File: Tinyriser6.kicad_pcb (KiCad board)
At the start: 4 copper layers, 113.2 x 23.5 mm, 25 parts, among them J1 Bus_M.2_Socket_M, J2 Bus_PCI_Express_x16, J3 Conn_02x04_Odd_Even, J6 USB_A, J7 Conn_02x10_Odd_Even, M1 Fan_4pin

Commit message: finished connecting pretty much all of the random io
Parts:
- moved J7 18.1 mm to (184.2, 66.0), turned to -90 degrees
- moved TP3 8.30 mm to (155.6, 55.5)
- moved TP7 8.30 mm to (155.6, 58.5)
- moved G*** 3.95 mm to (139.9, 66.5) (x2)
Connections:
- J7 pad 1: RSMRST_SIO# -> GND
- J7 pad 10: PWRBTN# -> PCIe_CPU_REFCLK11+
- J7 pad 11: PCIe_CPU_REFCLK11+ -> PWRBTN#
- J7 pad 12: ME_RECOVERY_BMC -> PCIe_CPU_REFCLK11-
- J7 pad 13: FP_RST# -> AZ_SDOUT_R
- J7 pad 14: SMLINK1_DATA -> SIO_SML1ALERT#
- J7 pad 15: SMLINK1_CLK -> GPU_PWR_EN
- J7 pad 16: PCIE_X8_X4_PRSNT# -> GPU_MACO_EN
- J7 pad 17: +3V3_S5 -> PCH_SYSPOWEROK
- J7 pad 18: +3V3 -> BMC_DETECT#
- J7 pad 19: GND -> +5V
- J7 pad 2: +5V -> GND
- J7 pad 20: GND -> RSMRST_SIO#
- J7 pad 3: BMC_DETECT# -> +3V3
- J7 pad 4: PCH_SYSPOWEROK -> +3V3_S5
- J7 pad 5: GPU_MACO_EN -> PCIE_X8_X4_PRSNT#
- J7 pad 6: GPU_PWR_EN -> SMLINK1_CLK
- J7 pad 7: SIO_SML1ALERT# -> SMLINK1_DATA
- J7 pad 8: AZ_SDOUT_R -> FP_RST#
- J7 pad 9: PCIe_CPU_REFCLK11- -> ME_RECOVERY_BMC
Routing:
- net PCH_SYSPOWEROK: track 0.00 -> 51.7 mm
- net RSMRST_SIO#: track 1.80 -> 52.8 mm, vias 1 -> 2
- net BMC_DETECT#: track 0.00 -> 49.5 mm
- net PCIe_PCH_CLKREQ#: track 83.9 -> 84.6 mm

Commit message: UNROUTED 0 LETS GOOOO
lots of tweaks left to make though :3
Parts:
- moved G*** 18.3 mm to (126.2, 54.5) (x2)
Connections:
- TP3 pad 1: +3V3 -> unconnected-(TP3-Pad1)
- TP7 pad 1: GND -> unconnected-(TP7-Pad1)
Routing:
- net PCIe_PCH_Rx2-: track 65.0 -> 66.6 mm
- net PCIe_PCH_Rx2+: track 65.9 -> 67.5 mm
- net PCIe_PCH_Rx0-: track 47.1 -> 48.7 mm
- net PCIe_PCH_Rx0+: track 48.0 -> 49.6 mm
- net GND: vias 6 -> 36
- net +5V: vias 0 -> 7
- added copper zone on In1.Cu, net +5V
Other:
- board text added: "TODO: [x] move pcie slot down 0.25mm [ ] change usb footprint [ ] fix logos [x] somehow make the random io fit [ ] look into m.2 slot placement [ ] ground vias!!!!!!!!!! [ ] final silkscreen check"
- board text removed: "TODO: [x] move pcie slot down 0.25mm [ ] change usb footprint [ ] fix logos [ ] somehow make the random io fit [ ] look into m.2 slot placement [ ] ground vias!!!!!!!!!! [ ] final silkscreen check"

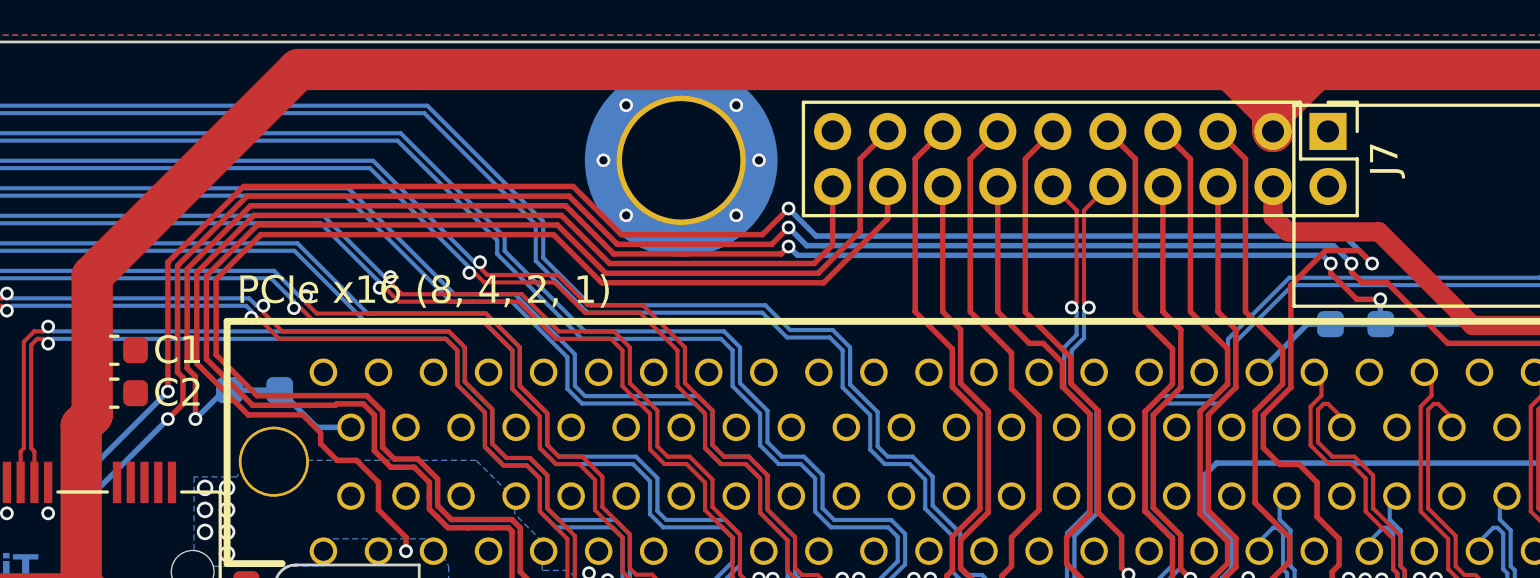
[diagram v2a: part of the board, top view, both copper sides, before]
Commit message: routed 5V rail properly
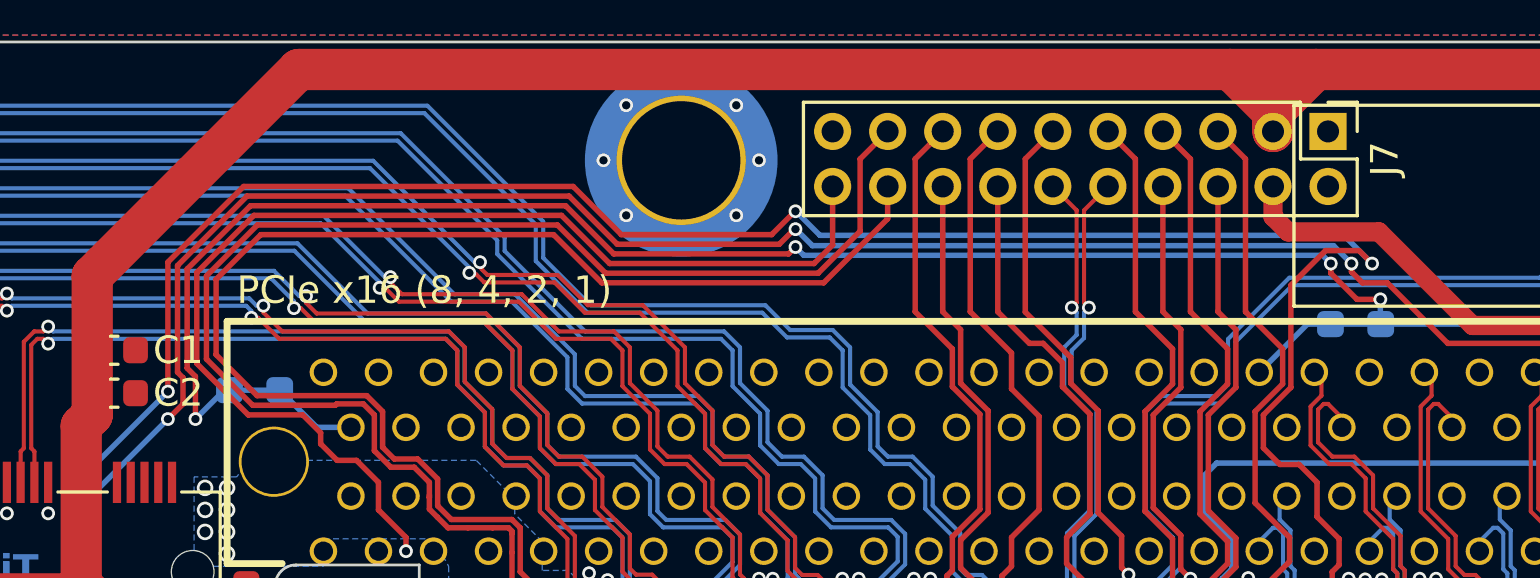
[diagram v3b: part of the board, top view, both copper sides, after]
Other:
- board text added: "meow"

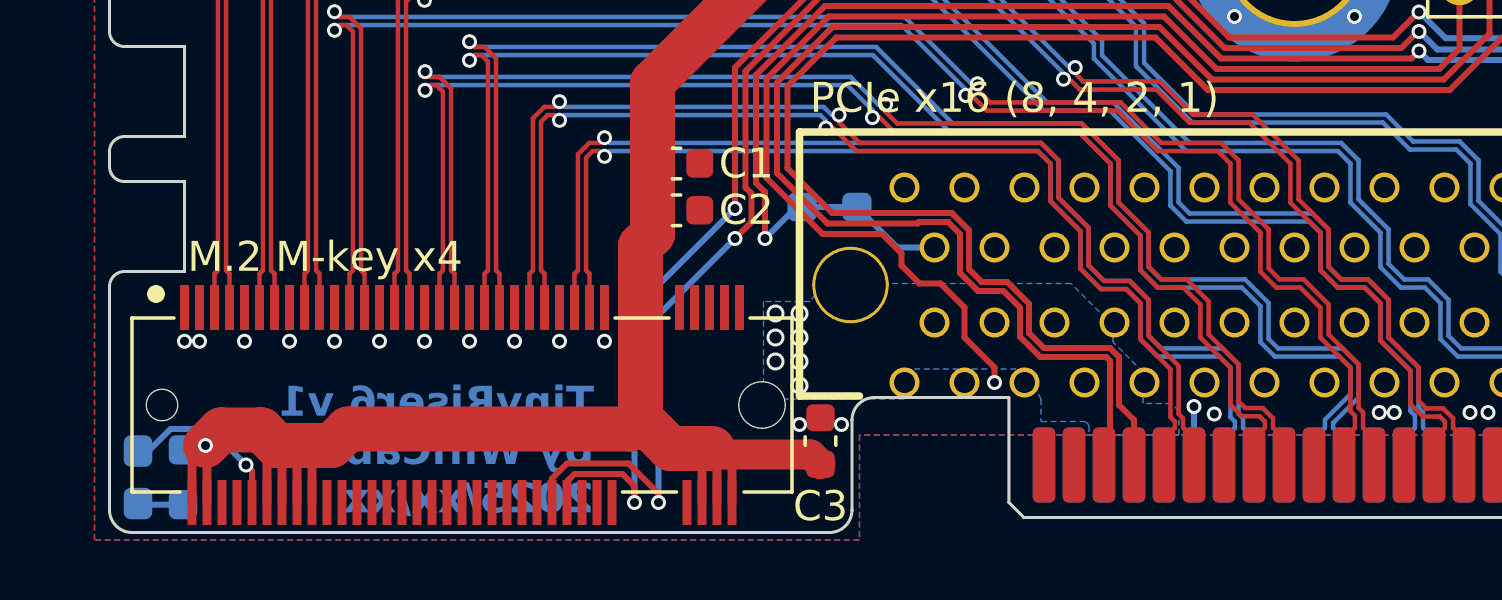
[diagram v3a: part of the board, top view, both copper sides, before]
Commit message: added ground keepout zones
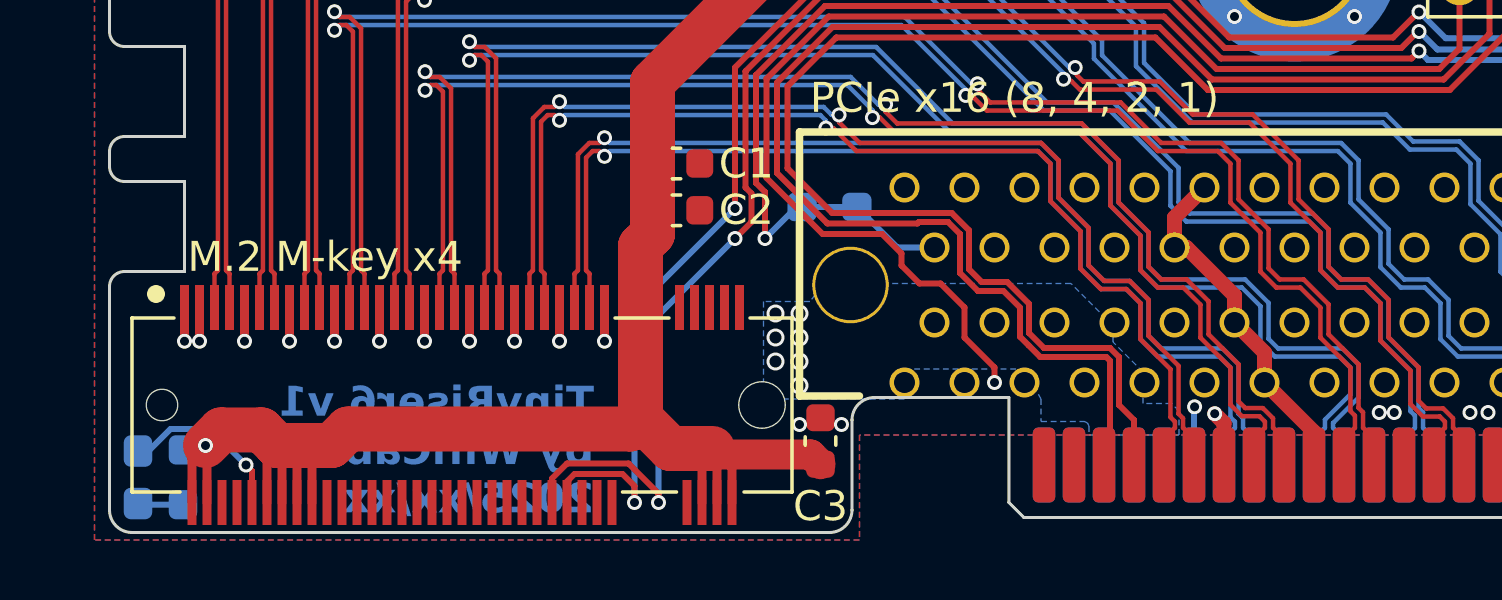
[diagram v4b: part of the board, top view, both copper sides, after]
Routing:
- net GND: track 0.00 -> 26.0 mm
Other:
- board text added: "TODO: [x] move pcie slot down 0.25mm [ ] change usb footprint [ ] fix logos [x] somehow make the random io fit [ ] look into m.2 slot placement [ ] ground vias!!!!!!!!!! [ ] final silkscreen check [ ] wiggles"
- board text removed: "TODO: [x] move pcie slot down 0.25mm [ ] change usb footprint [ ] fix logos [x] somehow make the random io fit [ ] look into m.2 slot placement [ ] ground vias!!!!!!!!!! [ ] final silkscreen check"

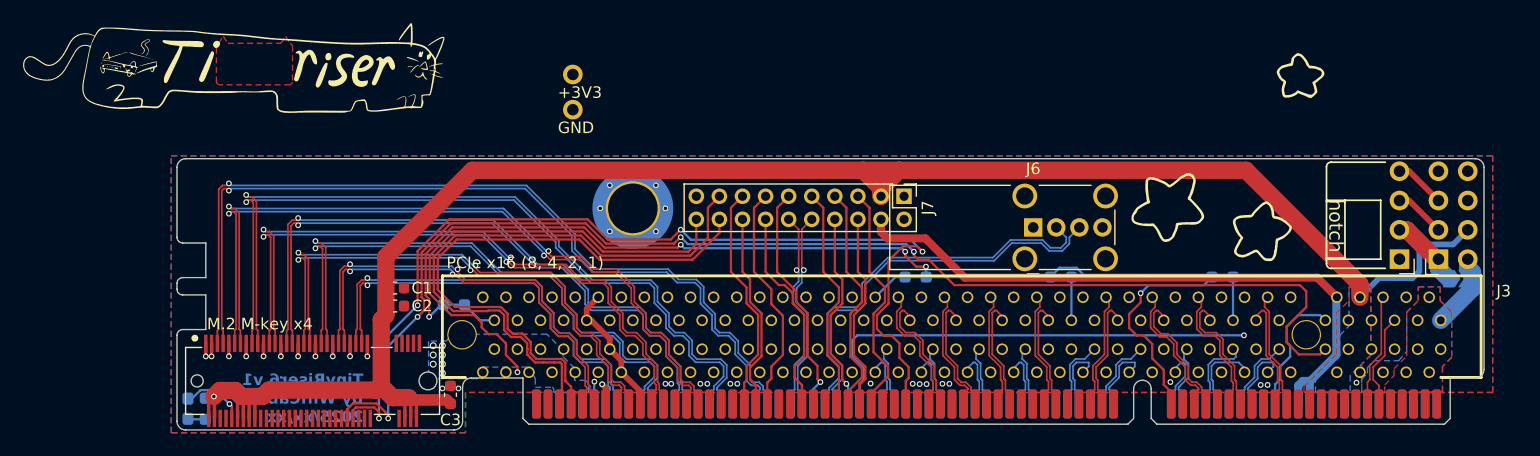
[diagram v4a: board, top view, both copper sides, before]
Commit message: ran some ground, added PCH lane wiggles
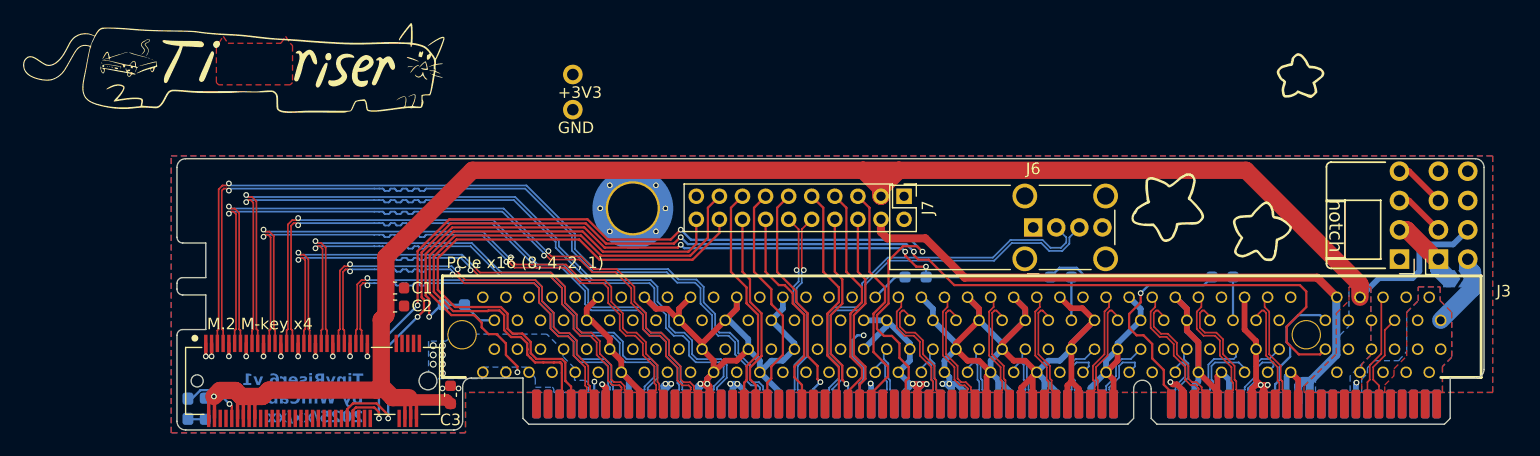
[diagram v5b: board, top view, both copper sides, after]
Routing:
- net GND: track 26.0 -> 287.1 mm
- net PCIe_PCH_Rx2-: track 66.6 -> 67.5 mm
- net PCIe_PCH_Rx1+: track 54.6 -> 55.5 mm
- net PCIe_PCH_Rx0-: track 48.7 -> 49.6 mm
- net PCIe_PCH_Tx3-: track 63.0 -> 63.9 mm
- net PCIe_PCH_Tx2-: track 54.4 -> 55.2 mm
- net PCIe_PCH_Rx3+: track 72.5 -> 73.4 mm
- net PCIe_PCH_Tx1-: track 45.3 -> 46.2 mm
- net PCIe_PCH_Tx0+: track 36.7 -> 37.5 mm
- net PCIe_PCH_REFCLK+: track 35.4 -> 36.2 mm
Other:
- board text added: "TODO: [x] move pcie slot down 0.25mm [ ] change usb footprint [ ] fix logos [x] somehow make the random io fit [ ] look into m.2 slot placement [ ] ground vias!!!!!!!!!! [ ] final silkscreen check [x] wiggles"
- board text removed: "TODO: [x] move pcie slot down 0.25mm [ ] change usb footprint [ ] fix logos [x] somehow make the random io fit [ ] look into m.2 slot placement [ ] ground vias!!!!!!!!!! [ ] final silkscreen check [ ] wiggles"

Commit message: fixed some layer conflicts
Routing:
- net PERST#: track 159.0 -> 172.1 mm
- net PCIe_CPU_CLKREQ#: track 119.9 -> 132.7 mm
- net PCIe_PCH_CLKREQ#: track 84.6 -> 96.9 mm
- net PCIe_CPU_REFCLK11+: track 17.5 -> 17.4 mm, vias 1 -> 0
- net PCIe_CPU_REFCLK11-: track 17.5 -> 17.4 mm, vias 1 -> 0
